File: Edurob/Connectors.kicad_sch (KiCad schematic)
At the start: 18 parts, among them J1 Conn_01x03_Male, J1 OLED, J12 Conn_01x06_Pin, J13 Conn_01x06_Pin, J14 Conn_01x06_Pin, J16 Conn_01x20_Pin, J17 Conn_01x20_Pin, J2 Conn_01x03_Male, J2 Conn_01x04_Pin, J3 Conn_01x03_Male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

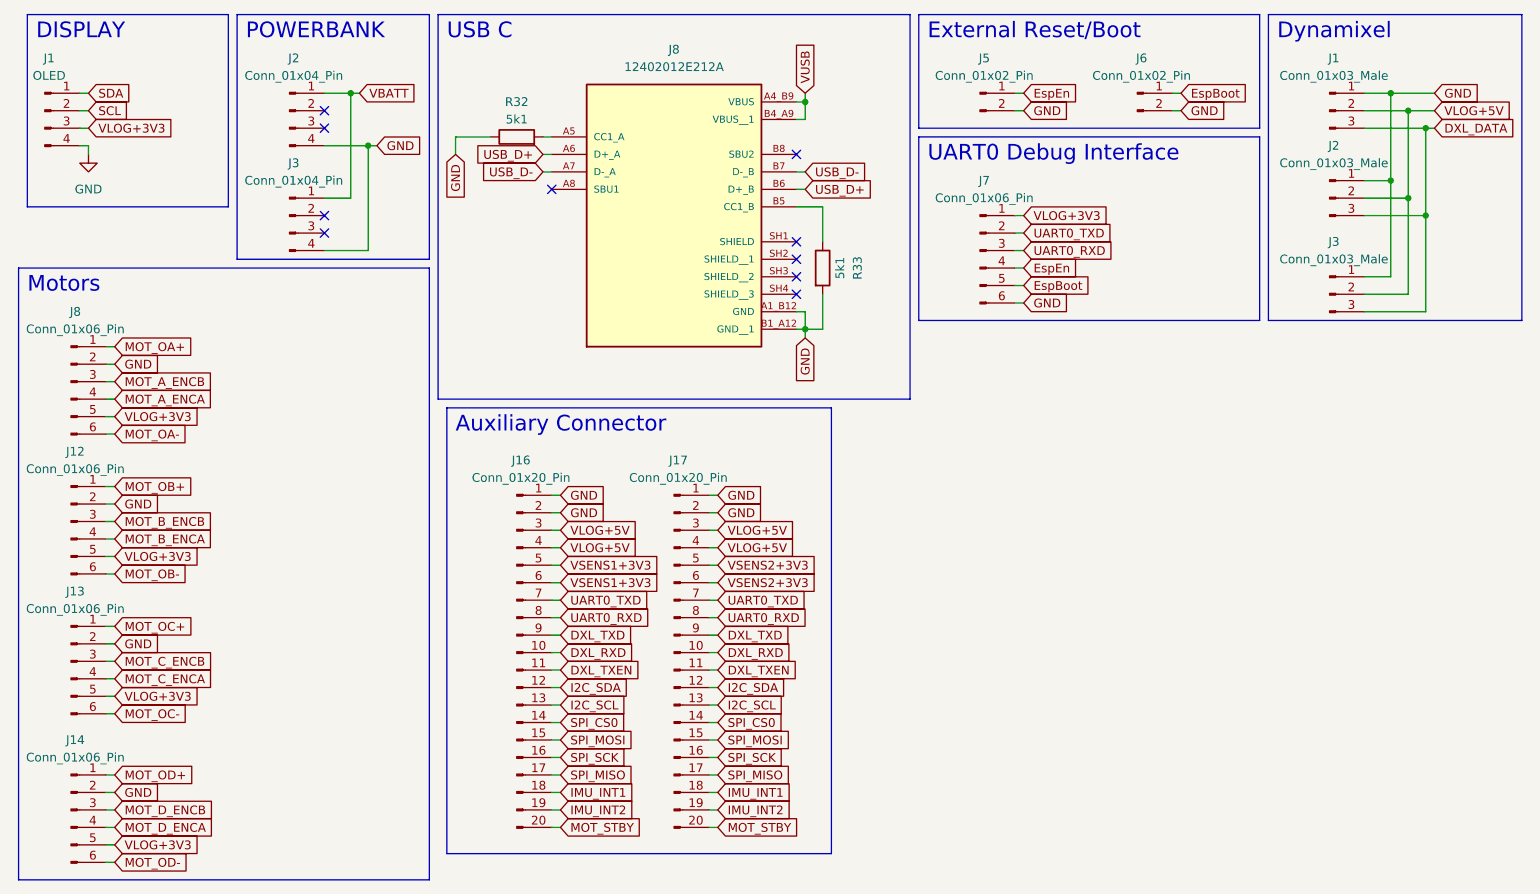
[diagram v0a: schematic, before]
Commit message: Added GPIO Expander, finalized Connector positions
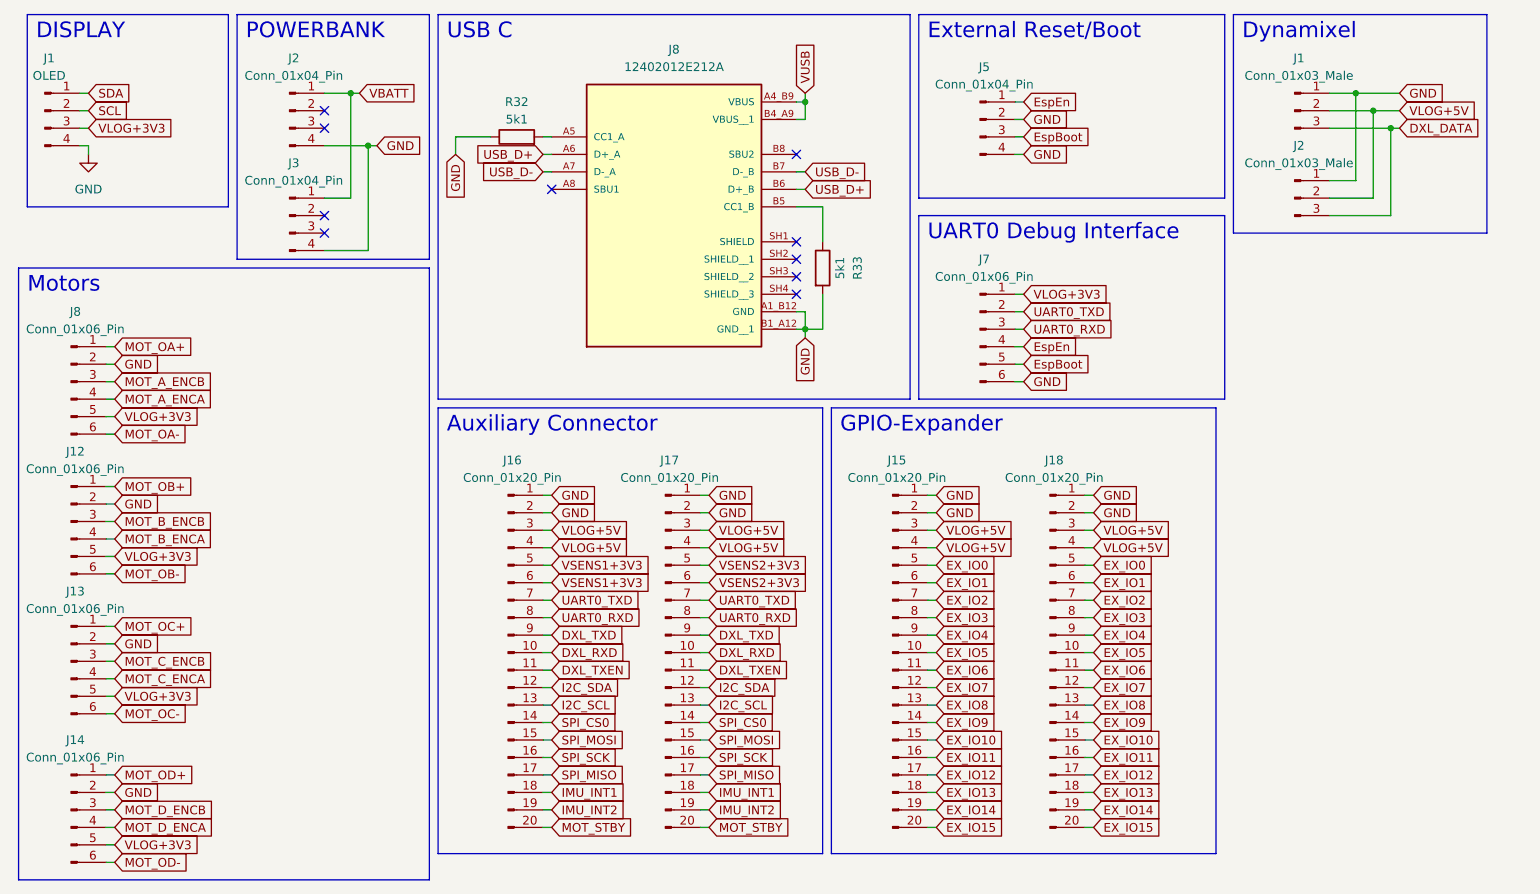
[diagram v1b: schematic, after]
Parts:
- removed J3: Conn_01x03_Male, Connector_JST:JST_EH_B3B-EH-A_1x03_P2.50mm_Vertical, symbol Connector:Conn_01x03_Male
- removed J5, J6: Conn_01x02_Pin, Connector_PinSocket_2.54mm:PinSocket_1x02_P2.54mm_Horizontal, symbol Connector:Conn_01x02_Pin
- added J15, J18: Conn_01x20_Pin, Connector_PinSocket_2.54mm:PinSocket_2x10_P2.54mm_Vertical, symbol Connector:Conn_01x20_Pin
- added J5: Conn_01x04_Pin, Connector_PinSocket_2.54mm:PinSocket_1x04_P2.54mm_Horizontal, symbol Connector:Conn_01x04_Pin
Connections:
- net EspBoot: now also J5.3 (Pin_3)
- net EspEn: now also J5.1 (Pin_1)
- net GND: now also J15.1 (Pin_1), J15.2 (Pin_2), J18.1 (Pin_1), J18.2 (Pin_2), J5.2 (Pin_2), J5.4 (Pin_4)
- net VLOG+5V: now also J15.3 (Pin_3), J15.4 (Pin_4), J18.3 (Pin_3), J18.4 (Pin_4)
- new net EX_IO0: J15.5 (Pin_5), J18.5 (Pin_5)
- new net EX_IO1: J15.6 (Pin_6), J18.6 (Pin_6)
- new net EX_IO10: J15.15 (Pin_15), J18.15 (Pin_15)
- new net EX_IO11: J15.16 (Pin_16), J18.16 (Pin_16)
- new net EX_IO12: J15.17 (Pin_17), J18.17 (Pin_17)
- new net EX_IO13: J15.18 (Pin_18), J18.18 (Pin_18)
- new net EX_IO14: J15.19 (Pin_19), J18.19 (Pin_19)
- new net EX_IO15: J15.20 (Pin_20), J18.20 (Pin_20)
- new net EX_IO2: J15.7 (Pin_7), J18.7 (Pin_7)
- new net EX_IO3: J15.8 (Pin_8), J18.8 (Pin_8)
- new net EX_IO4: J15.9 (Pin_9), J18.9 (Pin_9)
- new net EX_IO5: J15.10 (Pin_10), J18.10 (Pin_10)
- new net EX_IO6: J15.11 (Pin_11), J18.11 (Pin_11)
- new net EX_IO7: J15.12 (Pin_12), J18.12 (Pin_12)
- new net EX_IO8: J15.13 (Pin_13), J18.13 (Pin_13)
- new net EX_IO9: J15.14 (Pin_14), J18.14 (Pin_14)
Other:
- note added: "GPIO-Expander"
- moved on the sheet: J1, J16, J17, J2, J7

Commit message: Finalized part placement
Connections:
- net EspBoot: now also J7.4 (Pin_4); no longer J7.5 (Pin_5)
- net EspEn: now also J7.5 (Pin_5); no longer J7.4 (Pin_4)
- net IMU_INT1: now also J16.14 (Pin_14), J17.14 (Pin_14); no longer J16.18 (Pin_18), J17.18 (Pin_18)
- net SPI_CS0: now also J16.18 (Pin_18), J17.18 (Pin_18); no longer J16.14 (Pin_14), J17.14 (Pin_14)
- net SPI_MISO: now also J16.15 (Pin_15), J17.15 (Pin_15); no longer J16.17 (Pin_17), J17.17 (Pin_17)
- net SPI_MOSI: now also J16.17 (Pin_17), J17.17 (Pin_17); no longer J16.15 (Pin_15), J17.15 (Pin_15)
- net UART0_RXD: now also J16.7 (Pin_7), J17.7 (Pin_7); no longer J16.8 (Pin_8), J17.8 (Pin_8)
- net UART0_TXD: now also J16.8 (Pin_8), J17.8 (Pin_8); no longer J16.7 (Pin_7), J17.7 (Pin_7)

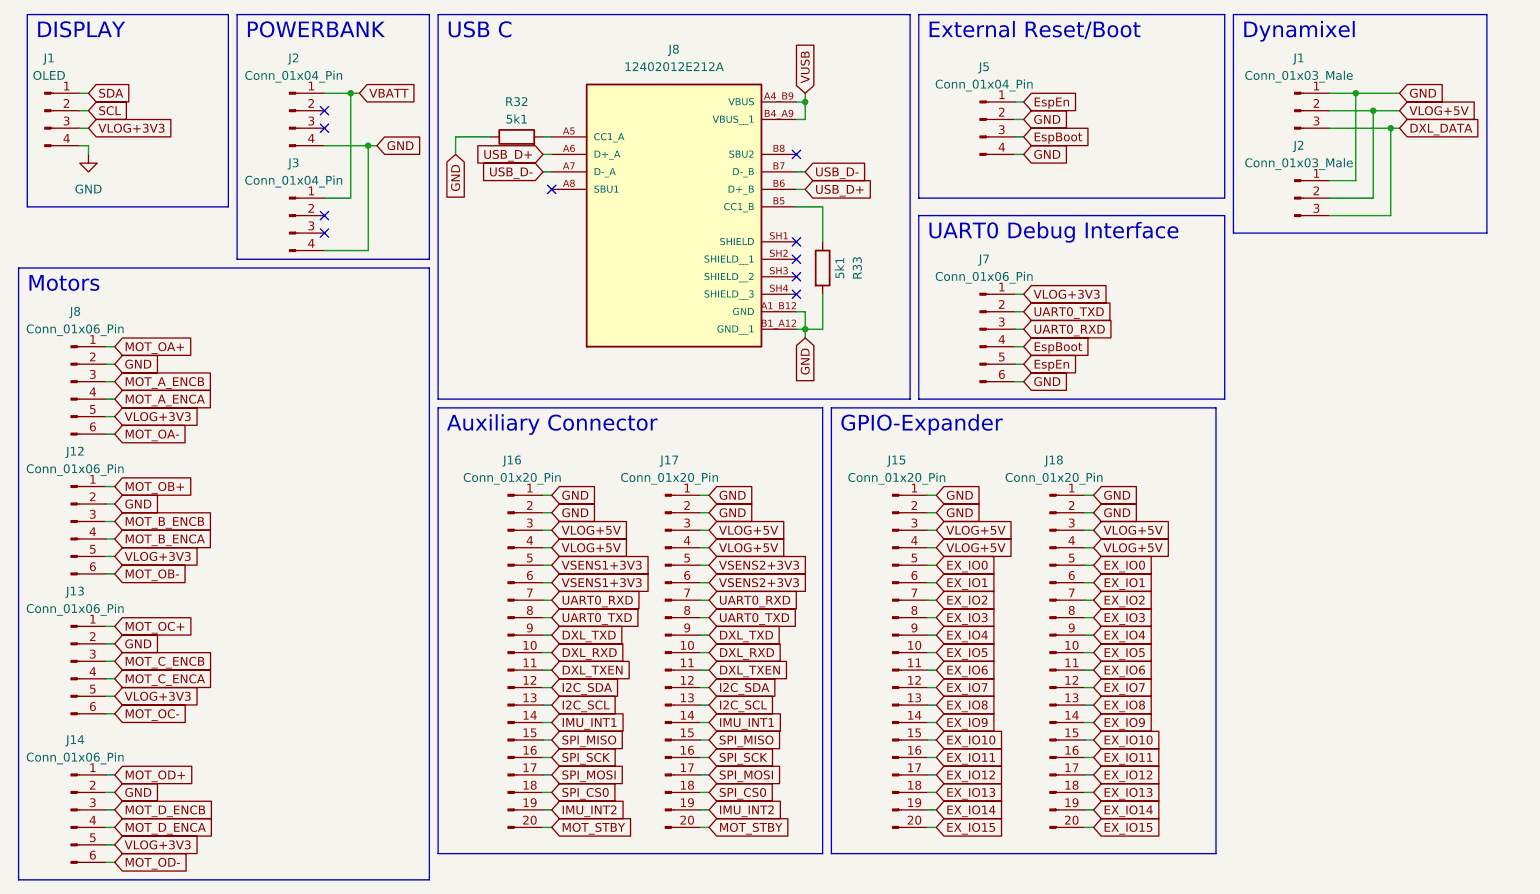
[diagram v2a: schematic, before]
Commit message: Finished routing and part placement
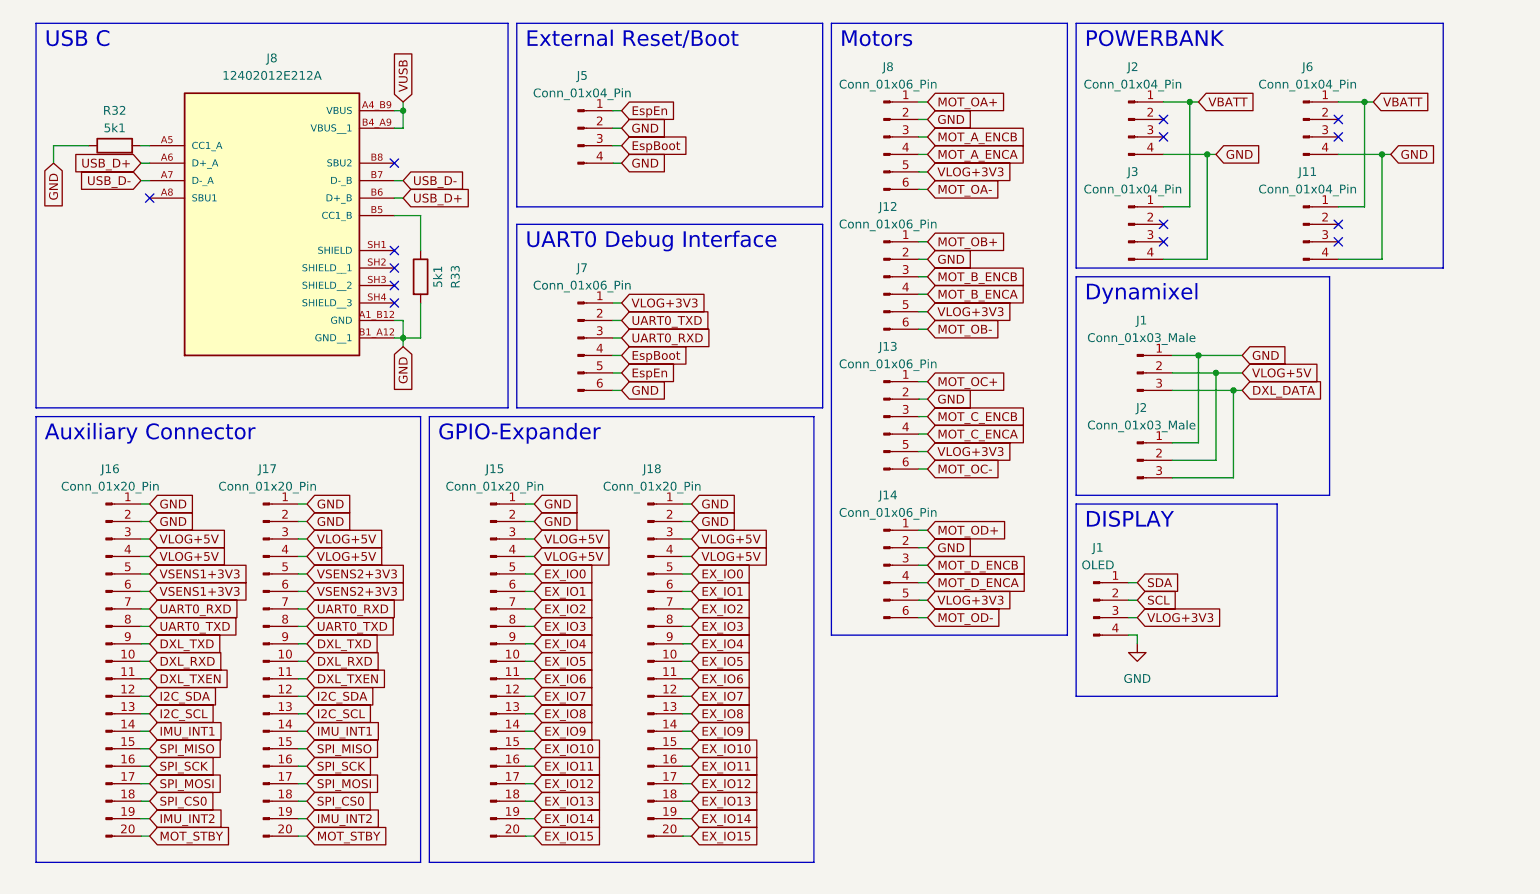
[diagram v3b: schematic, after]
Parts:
- added J11, J6: Conn_01x04_Pin, Connector_PinSocket_2.54mm:PinSocket_1x04_P2.54mm_Vertical, symbol Connector:Conn_01x04_Pin
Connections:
- net GND: now also J11.4 (Pin_4), J6.4 (Pin_4)
- net VBATT: now also J11.1 (Pin_1), J6.1 (Pin_1)
- no-connect marks 10 -> 14
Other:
- moved on the sheet: J1, J12, J13, J14, J15, J16, J17, J18, J2, J3, J5, J7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

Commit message: Release v1.0.1
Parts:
- J1, J11, J12, J13, J14, J15, J16, J17, J18, J2, J3, J5, J6, J7, J8: Placed (none) -> False
- J8: MANUFACTURER Amphenol -> (none); MAXIMUM_PACKAGE_HEIGHT 3.26 mm -> (none); Manufacturer_Name (none) -> Amphenol; Manufacturer_Part_Number (none) -> 12402012E212A; Mouser Part Number (none) -> 523-12402012E212A; Mouser Price/Stock (none) -> https://www.mouser.de/ProductDetail/523-12402012E212A; PARTREV 4 -> (none); Placed (none) -> True; STANDARD Manufacturer Recommendations -> (none)
- R32, R33: Manufacturer_Name (none) -> TE Connectivity / Holsworthy; Manufacturer_Part_Number (none) -> CRG0603F5K1; Mouser Part Number (none) -> 279-CRG0603F5K1; Mouser Price/Stock (none) -> https://www.mouser.de/ProductDetail/279-CRG0603F5K1; Placed (none) -> True
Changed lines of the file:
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@@
+      (effects (font (size 1.27 1.27)) hide)
+    )
+    (property "Placed" "False" (at 25.4 107.95 0)
       (effects (font (size 1.27 1.27)) hide)
     )
@@
       (effects (font (size 1.27 1.27)) hide)
     )
+    (property "Placed" "False" (at 104.14 107.95 0)
+      (effects (font (size 1.27 1.27)) hide)
+    )
     (pin "3")
     (pin "14")
@@
       (effects (font (size 1.27 1.27)) hide)
     )
+    (property "Placed" "False" (at 138.43 93.98 0)
+      (effects (font (size 1.27 1.27)) hide)
+    )
     (pin "5")
     (pin "2")
@@
     )
     (property "Datasheet" "~" (at 168.91 99.06 0)
+      (effects (font (size 1.27 1.27)) hide)
+    )
+    (property "Placed" "False" (at 168.91 99.06 0)
       (effects (font (size 1.27 1.27)) hide)
     )
@@
       (effects (font (size 1.27 1.27)) hide)
     )
+    (property "Placed" "False" (at 173.99 29.21 0)
+      (effects (font (size 1.27 1.27)) hide)
+    )
     (pin "3")
     (pin "1")
@@
       (effects (font (size 1.27 1.27)) (justify bottom) hide)
     )
-    (property "Datasheet" "" (at 49.53 38.1 0)
-      (effects (font (size 1.27 1.27)) hide)
-    )
-    (property "PARTREV" "4" (at 49.53 38.1 0)
-      (effects (font (size 1.27 1.27)) (justify bottom) hide)
-    )
-    (property "STANDARD" "Manufacturer Recommendations" (at 49.53 38.1 0)
-      (effects (font (size 1.27 1.27)) (justify bottom) hide)
-    )
-    (property "MAXIMUM_PACKAGE_HEIGHT" "3.26 mm" (at 49.53 38.1 0)
-      (effects (font (size 1.27 1.27)) (justify bottom) hide)
-    )
-    (property "MANUFACTURER" "Amphenol" (at 49.53 38.1 0)
-      (effects (font (size 1.27 1.27)) (justify bottom) hide)
+    (property "Datasheet" "https://cdn.amphenol-cs.com/media/wysiwyg/files/documentation/datasheet/inputoutput/io_usb_type_c.pdf" (at 49.53 38.1 0)
+      (effects (font (size 1.27 1.27)) hide)
+    )
+    (property "Manufacturer_Name" "Amphenol" (at 49.53 38.1 0)
+      (effects (font (size 1.27 1.27)) hide)
+    )
+    (property "Manufacturer_Part_Number" "12402012E212A" (at 49.53 38.1 0)
+      (effects (font (size 1.27 1.27)) hide)
+    )
+    (property "Mouser Part Number" "523-12402012E212A" (at 49.53 38.1 0)
+      (effects (font (size 1.27 1.27)) hide)
+    )
+    (property "Mouser Price/Stock" "https://www.mouser.de/ProductDetail/523-12402012E212A" (at 49.53 38.1 0)
+      (effects (font (size 1.27 1.27)) hide)
+    )
+    (property "Placed" "True" (at 49.53 38.1 0)
+      (effects (font (size 1.27 1.27)) hide)
     )
     (pin "A1_B12")
@@
       (effects (font (size 1.27 1.27)) hide)
     )
+    (property "Placed" "False" (at 93.98 30.48 0)
+      (effects (font (size 1.27 1.27)) hide)
+    )
     (pin "2")
     (pin "3")
@@
     )
     (property "Datasheet" "~" (at 199.39 44.45 0)
+      (effects (font (size 1.27 1.27)) hide)
+    )
+    (property "Placed" "False" (at 199.39 44.45 0)
       (effects (font (size 1.27 1.27)) hide)
     )
@@
       (effects (font (size 1.27 1.27)) hide)
     )
+    (property "Manufacturer_Name" "TE Connectivity / Holsworthy" (at 71.12 52.07 0)
+      (effects (font (size 1.27 1.27)) hide)
+    )
+    (property "Manufacturer_Part_Number" "CRG0603F5K1" (at 71.12 52.07 0)
+      (effects (font (size 1.27 1.27)) hide)
+    )
+    (property "Mouser Part Number" "279-CRG0603F5K1" (at 71.12 52.07 0)
+      (effects (font (size 1.27 1.27)) hide)
+    )
+    (property "Mouser Price/Stock" "https://www.mouser.de/ProductDetail/279-CRG0603F5K1" (at 71.12 52.07 0)
+      (effects (font (size 1.27 1.27)) hide)
+    )
+    (property "Placed" "True" (at 71.12 52.07 0)
+      (effects (font (size 1.27 1.27)) hide)
+    )
     (pin "1")
     (pin "2")
@@
       (effects (font (size 1.27 1.27)) hide)
     )
+    (property "Placed" "False" (at 93.98 60.96 0)
+      (effects (font (size 1.27 1.27)) hide)
+    )
     (pin "4")
     (pin "1")
@@
     )
     (property "Datasheet" "~" (at 48.26 107.95 0)
+      (effects (font (size 1.27 1.27)) hide)
+    )
+    (property "Placed" "False" (at 48.26 107.95 0)
       (effects (font (size 1.27 1.27)) hide)
     )
@@
       (effects (font (size 1.27 1.27)) hide)
     )
+    (property "Placed" "False" (at 138.43 72.39 0)
+      (effects (font (size 1.27 1.27)) hide)
+    )
     (pin "5")
     (pin "2")
@@
       (effects (font (size 1.27 1.27)) hide)
     )
+    (property "Placed" "False" (at 173.99 44.45 0)
+      (effects (font (size 1.27 1.27)) hide)
+    )
     (pin "1")
     (pin "2")
@@
       (effects (font (size 1.27 1.27)) hide)
     )
+    (property "Placed" "False" (at 138.43 31.75 0)
+      (effects (font (size 1.27 1.27)) hide)
+    )
     (pin "5")
     (pin "2")
@@
     )
     (property "Datasheet" "~" (at 175.26 66.04 0)
+      (effects (font (size 1.27 1.27)) hide)
+    )
+    (property "Placed" "False" (at 175.26 66.04 0)
       (effects (font (size 1.27 1.27)) hide)
     )
@@
       (effects (font (size 1.27 1.27)) hide)
     )
+    (property "Placed" "False" (at 199.39 29.21 0)
+      (effects (font (size 1.27 1.27)) hide)
+    )
     (pin "3")
     (pin "1")
@@
     )
     (property "Datasheet" "~" (at 81.28 107.95 0)
+      (effects (font (size 1.27 1.27)) hide)
+    )
+    (property "Placed" "False" (at 81.28 107.95 0)
       (effects (font (size 1.27 1.27)) hide)
     )
@@
       (effects (font (size 1.27 1.27)) hide)
     )
+    (property "Manufacturer_Name" "TE Connectivity / Holsworthy" (at 26.67 33.02 0)
+      (effects (font (size 1.27 1.27)) hide)
+    )
+    (property "Manufacturer_Part_Number" "CRG0603F5K1" (at 26.67 33.02 0)
+      (effects (font (size 1.27 1.27)) hide)
+    )
+    (property "Mouser Part Number" "279-CRG0603F5K1" (at 26.67 33.02 0)
+      (effects (font (size 1.27 1.27)) hide)
+    )
+    (property "Mouser Price/Stock" "https://www.mouser.de/ProductDetail/279-CRG0603F5K1" (at 26.67 33.02 0)
+      (effects (font (size 1.27 1.27)) hide)
+    )
+    (property "Placed" "True" (at 26.67 33.02 0)
+      (effects (font (size 1.27 1.27)) hide)
+    )
     (pin "1")
     (pin "2")
@@
       (effects (font (size 1.27 1.27)) hide)
     )
+    (property "Placed" "False" (at 175.26 78.74 0)
+      (effects (font (size 1.27 1.27)) hide)
+    )
     (pin "1")
     (pin "2")
@@
       (effects (font (size 1.27 1.27)) hide)
     )
+    (property "Placed" "False" (at 138.43 52.07 0)
+      (effects (font (size 1.27 1.27)) hide)
+    )
